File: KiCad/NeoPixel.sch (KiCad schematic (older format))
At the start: 13 parts, among them J701 NEO1, J702 5V_I/O_2, J703 5V_I/O_1, J704 NEO1, J705 NEO1, J706 NEO1, J707 NeoPixel, U701 TXB0102DCT

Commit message: Remade layout
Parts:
- removed J707: NeoPixel, Pin_Headers:Pin_Header_Straight_1x01_Pitch2.54mm, symbol CONN_01X01
- added J707: CONN_01X03, Pin_Headers:Pin_Header_Straight_1x03_Pitch2.54mm, symbol CONN_01X03
- J704: value NEO1 -> NEO2
- J705: value NEO1 -> NEO3
- J706: value NEO1 -> NEO4
- renumbered J702 to J701, J703 to J702, J701 to J703
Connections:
- net GND: now also J701.1 (P1), J702.1 (P1), J707.1 (P1); no longer J701.2 (P2), J702.2 (P2)
- net POWER5V: now also J707.2 (P2)
- net at C703.1, U701.1 (B2): now also J701.2 (P2); no longer J701.1 (P1)
- net at C704.1, J703.1, U701.8 (B1): now also J702.2 (P2); no longer J702.1 (P1)
- net at J706.4: now also J707.3 (P3)
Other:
- moved on the sheet: C703, C704, J701, J702, J703, J704, J705, J706

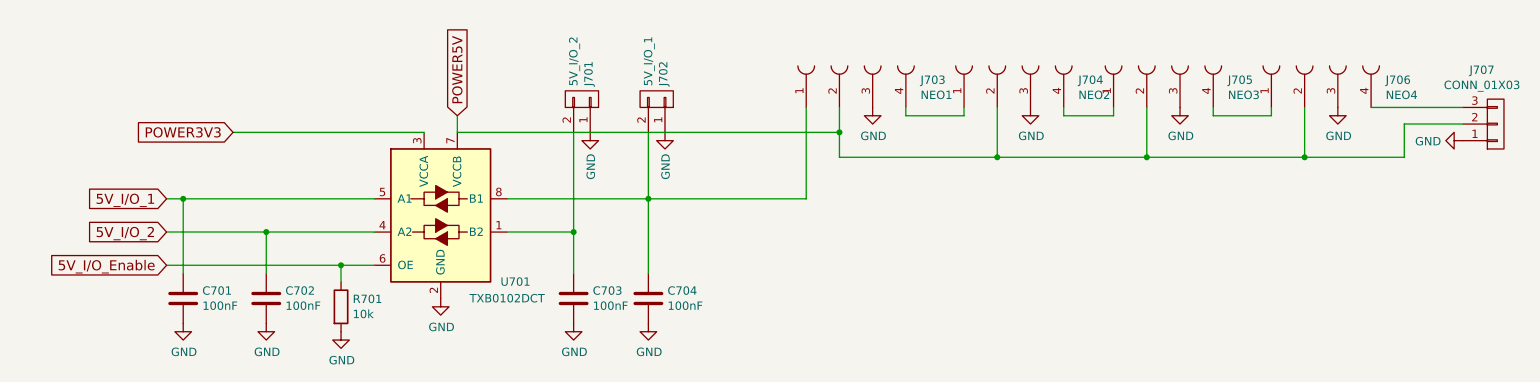
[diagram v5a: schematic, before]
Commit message: New sense input circuits. New layout
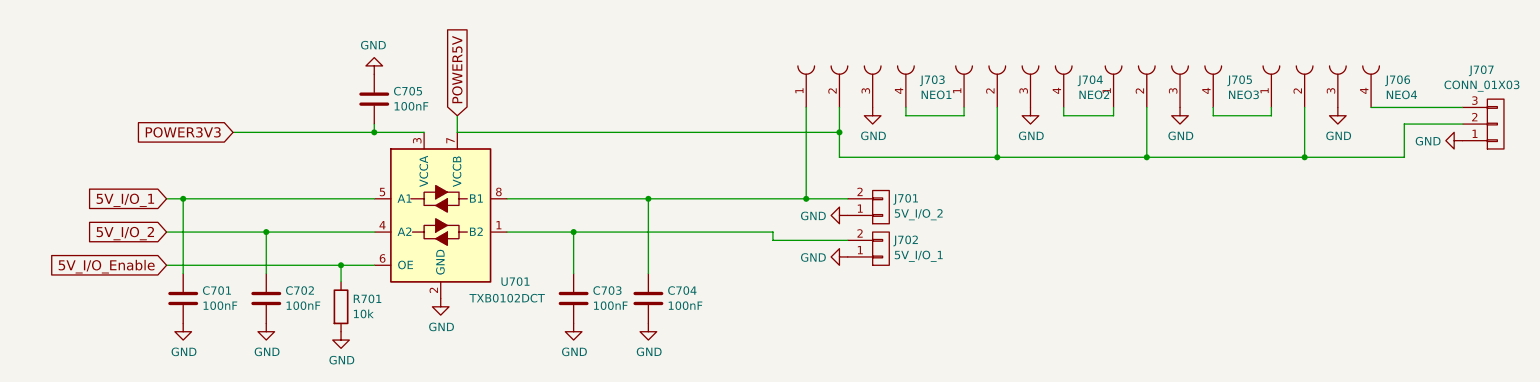
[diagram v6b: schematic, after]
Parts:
- added C705: 100nF, Capacitors_SMD:C_0805, symbol C
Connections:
- net GND: now also C705.1
- net POWER3V3: now also C705.2
- net at C703.1, U701.1 (B2): now also J702.2 (P2); no longer J701.2 (P2)
- net at C704.1, J703.1, U701.8 (B1): now also J701.2 (P2); no longer J702.2 (P2)
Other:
- moved on the sheet: J701, J702
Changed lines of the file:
@@
 F 1 "TXB0102DCT" H 3450 1200 50  0000 C CNN
 F 2 "Housings_SSOP:TSSOP-8_3x3mm_Pitch0.65mm" H 4000 1100 50  0001 C CNN
-F 3 "" H 3050 1670 50  0001 C CNN
+F 3 "https://www.digikey.se/product-detail/en/texas-instruments/TXB0102DCUR/296-22862-1-ND/1740009" H 3050 1670 50  0001 C CNN
 	1    3050 1700
 	1    0    0    -1
@@
 POWER3V3
 $Comp
-L GND #PWR0136
+L GND #PWR0144
 U 1 1 5926005F
 P 3050 2200
-F 0 "#PWR0136" H 3050 1950 50  0001 C CNN
+F 0 "#PWR0144" H 3050 1950 50  0001 C CNN
 F 1 "GND" H 3055 2027 50  0000 C CNN
 F 2 "" H 3050 2200 50  0001 C CNN
@@
 $EndComp
 $Comp
-L GND #PWR0137
+L GND #PWR0145
 U 1 1 592606C6
 P 2450 2400
-F 0 "#PWR0137" H 2450 2150 50  0001 C CNN
+F 0 "#PWR0145" H 2450 2150 50  0001 C CNN
 F 1 "GND" H 2455 2227 50  0000 C CNN
 F 2 "" H 2450 2400 50  0001 C CNN
@@
 $EndComp
 $Comp
-L GND #PWR0138
+L GND #PWR0146
 U 1 1 59260916
 P 2000 2350
-F 0 "#PWR0138" H 2000 2100 50  0001 C CNN
+F 0 "#PWR0146" H 2000 2100 50  0001 C CNN
 F 1 "GND" H 2005 2177 50  0000 C CNN
 F 2 "" H 2000 2350 50  0001 C CNN
@@
 $EndComp
 $Comp
-L GND #PWR0139
+L GND #PWR0147
 U 1 1 592609AA
 P 1500 2350
-F 0 "#PWR0139" H 1500 2100 50  0001 C CNN
+F 0 "#PWR0147" H 1500 2100 50  0001 C CNN
 F 1 "GND" H 1505 2177 50  0000 C CNN
 F 2 "" H 1500 2350 50  0001 C CNN
@@
 $EndComp
 $Comp
-L GND #PWR0140
+L GND #PWR0148
 U 1 1 59260BC2
 P 3850 2350
-F 0 "#PWR0140" H 3850 2100 50  0001 C CNN
+F 0 "#PWR0148" H 3850 2100 50  0001 C CNN
 F 1 "GND" H 3855 2177 50  0000 C CNN
 F 2 "" H 3850 2350 50  0001 C CNN
@@
 $EndComp
 $Comp
-L GND #PWR0141
+L GND #PWR0149
 U 1 1 59260BD9
 P 4300 2350
-F 0 "#PWR0141" H 4300 2100 50  0001 C CNN
+F 0 "#PWR0149" H 4300 2100 50  0001 C CNN
 F 1 "GND" H 4305 2177 50  0000 C CNN
 F 2 "" H 4300 2350 50  0001 C CNN
@@
 L CONN_01X02 J702
 U 1 1 59260CEC
-P 4350 1000
-F 0 "J702" H 4428 1041 50  0000 L CNN
-F 1 "5V_I/O_1" H 4428 950 50  0000 L CNN
-F 2 "Pin_Headers:Pin_Header_Straight_1x02_Pitch2.54mm" H 4350 1000 50  0001 C CNN
-F 3 "" H 4350 1000 50  0001 C CNN
-	1    4350 1000
-	0    1    -1   0
+P 5700 1900
+F 0 "J702" H 5778 1849 50  0000 L CNN
+F 1 "5V_I/O_1" H 5778 1940 50  0000 L CNN
+F 2 "Pin_Headers:Pin_Header_Straight_1x02_Pitch2.54mm" H 5700 1900 50  0001 C CNN
+F 3 "" H 5700 1900 50  0001 C CNN
+	1    5700 1900
+	1    0    0    1
 $EndComp
 $Comp
 L CONN_01X02 J701
 U 1 1 59260D8E
-P 3900 1000
-F 0 "J701" H 3978 1041 50  0000 L CNN
-F 1 "5V_I/O_2" H 3978 950 50  0000 L CNN
-F 2 "Pin_Headers:Pin_Header_Straight_1x02_Pitch2.54mm" H 3900 1000 50  0001 C CNN
-F 3 "" H 3900 1000 50  0001 C CNN
-	1    3900 1000
-	0    1    -1   0
-$EndComp
-$Comp
-L GND #PWR0142
+P 5700 1650
+F 0 "J701" H 5778 1599 50  0000 L CNN
+F 1 "5V_I/O_2" H 5778 1690 50  0000 L CNN
+F 2 "Pin_Headers:Pin_Header_Straight_1x02_Pitch2.54mm" H 5700 1650 50  0001 C CNN
+F 3 "" H 5700 1650 50  0001 C CNN
+	1    5700 1650
+	1    0    0    1
+$EndComp
+$Comp
+L GND #PWR0150
 U 1 1 59260EBE
-P 3950 1200
-F 0 "#PWR0142" H 3950 950 50  0001 C CNN
-F 1 "GND" V 3955 1072 50  0000 R CNN
-F 2 "" H 3950 1200 50  0001 C CNN
-F 3 "" H 3950 1200 50  0001 C CNN
-	1    3950 1200
-	1    0    0    -1
-$EndComp
-$Comp
-L GND #PWR0143
+P 5500 1700
+F 0 "#PWR0150" H 5500 1450 50  0001 C CNN
+F 1 "GND" V 5505 1572 50  0000 R CNN
+F 2 "" H 5500 1700 50  0001 C CNN
+F 3 "" H 5500 1700 50  0001 C CNN
+	1    5500 1700
+	0    1    1    0
+$EndComp
+$Comp
+L GND #PWR0151
 U 1 1 59260EE1
-P 4400 1200
-F 0 "#PWR0143" H 4400 950 50  0001 C CNN
-F 1 "GND" V 4405 1072 50  0000 R CNN
-F 2 "" H 4400 1200 50  0001 C CNN
-F 3 "" H 4400 1200 50  0001 C CNN
-	1    4400 1200
-	1    0    0    -1
+P 5500 1950
+F 0 "#PWR0151" H 5500 1700 50  0001 C CNN
+F 1 "GND" V 5505 1822 50  0000 R CNN
+F 2 "" H 5500 1950 50  0001 C CNN
+F 3 "" H 5500 1950 50  0001 C CNN
+	1    5500 1950
+	0    1    1    0
 $EndComp
 $Comp
@@
 $EndComp
 $Comp
-L GND #PWR0144
+L GND #PWR0152
 U 1 1 5926162B
 P 5650 1050
-F 0 "#PWR0144" H 5650 800 50  0001 C CNN
+F 0 "#PWR0152" H 5650 800 50  0001 C CNN
 F 1 "GND" H 5655 877 50  0000 C CNN
 F 2 "" H 5650 1050 50  0001 C CNN
@@
 $EndComp
 $Comp
-L GND #PWR0145
+L GND #PWR0153
 U 1 1 59261C0C
 P 6600 1050
-F 0 "#PWR0145" H 6600 800 50  0001 C CNN
+F 0 "#PWR0153" H 6600 800 50  0001 C CNN
 F 1 "GND" H 6605 877 50  0000 C CNN
 F 2 "" H 6600 1050 50  0001 C CNN
@@
 $EndComp
 $Comp
-L GND #PWR0146
+L GND #PWR0154
 U 1 1 59261C2F
 P 7500 1050
-F 0 "#PWR0146" H 7500 800 50  0001 C CNN
+F 0 "#PWR0154" H 7500 800 50  0001 C CNN
 F 1 "GND" H 7505 877 50  0000 C CNN
 F 2 "" H 7500 1050 50  0001 C CNN
@@
 $EndComp
 $Comp
-L GND #PWR0147
+L GND #PWR0155
 U 1 1 59261C52
 P 8450 1050
-F 0 "#PWR0147" H 8450 800 50  0001 C CNN
+F 0 "#PWR0155" H 8450 800 50  0001 C CNN
 F 1 "GND" H 8455 877 50  0000 C CNN
 F 2 "" H 8450 1050 50  0001 C CNN
@@
 Connection ~ 1500 1600
 Wire Wire Line
-	3450 1800 3850 1800
-Wire Wire Line
-	3850 1200 3850 2050
-Wire Wire Line
-	3450 1600 5250 1600
-Wire Wire Line
-	4300 1200 4300 2050
-Connection ~ 4300 1600
+	3450 1800 5050 1800
+Wire Wire Line
+	3850 1800 3850 2050
+Wire Wire Line
+	3450 1600 5500 1600
 Connection ~ 3850 1800
 Wire Wire Line
@@
 	9200 1050 8650 1050
 $Comp
-L GND #PWR0148
+L GND #PWR0156
 U 1 1 59280C13
 P 9200 1250
-F 0 "#PWR0148" H 9200 1000 50  0001 C CNN
+F 0 "#PWR0156" H 9200 1000 50  0001 C CNN
 F 1 "GND" V 9205 1122 50  0000 R CNN
 F 2 "" H 9200 1250 50  0001 C CNN
@@
 	8850 1150 9200 1150
 Connection ~ 8250 1350
+$Comp
+L C C705
+U 1 1 5938371E
+P 2650 1000
+F 0 "C705" H 2765 1046 50  0000 L CNN
+F 1 "100nF" H 2765 955 50  0000 L CNN
+F 2 "Capacitors_SMD:C_0805" H 2688 850 50  0001 C CNN
+F 3 "" H 2650 1000 50  0001 C CNN
+	1    2650 1000
+	1    0    0    -1
+$EndComp
+Wire Wire Line
+	2650 1150 2650 1200
+Connection ~ 2650 1200
+$Comp
+L GND #PWR0157
+U 1 1 593838B5
+P 2650 850
+F 0 "#PWR0157" H 2650 600 50  0001 C CNN
+F 1 "GND" H 2655 677 50  0000 C CNN
+F 2 "" H 2650 850 50  0001 C CNN
+F 3 "" H 2650 850 50  0001 C CNN
+	1    2650 850
+	-1   0    0    1
+$EndComp
+Wire Wire Line
+	4300 2050 4300 1600
+Connection ~ 4300 1600
+Connection ~ 5250 1600
+Wire Wire Line
+	5050 1800 5050 1850
+Wire Wire Line
+	5050 1850 5500 1850
 $EndSCHEMATC

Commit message: Starting another routing pass
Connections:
- net 5V_I/O_1 renamed 5V_IO_1
- net 5V_I/O_2 renamed 5V_IO_2
- net 5V_I/O_Enable renamed 5V_IO_Enable
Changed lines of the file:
@@
 POWER3V3
 $Comp
-L GND #PWR0144
+L GND #PWR0142
 U 1 1 5926005F
 P 3050 2200
-F 0 "#PWR0144" H 3050 1950 50  0001 C CNN
+F 0 "#PWR0142" H 3050 1950 50  0001 C CNN
 F 1 "GND" H 3055 2027 50  0000 C CNN
 F 2 "" H 3050 2200 50  0001 C CNN
@@
 $EndComp
 Text GLabel 1400 1800 0    60   Input ~ 0
-5V_I/O_2
+5V_IO_2
 Text GLabel 1400 1600 0    60   Input ~ 0
-5V_I/O_1
+5V_IO_1
 Text GLabel 1400 2000 0    60   Input ~ 0
-5V_I/O_Enable
+5V_IO_Enable
 $Comp
 L R R701
@@
 $EndComp
 $Comp
-L GND #PWR0145
+L GND #PWR0143
 U 1 1 592606C6
 P 2450 2400
-F 0 "#PWR0145" H 2450 2150 50  0001 C CNN
+F 0 "#PWR0143" H 2450 2150 50  0001 C CNN
 F 1 "GND" H 2455 2227 50  0000 C CNN
 F 2 "" H 2450 2400 50  0001 C CNN
@@
 $EndComp
 $Comp
-L GND #PWR0146
+L GND #PWR0144
 U 1 1 59260916
 P 2000 2350
-F 0 "#PWR0146" H 2000 2100 50  0001 C CNN
+F 0 "#PWR0144" H 2000 2100 50  0001 C CNN
 F 1 "GND" H 2005 2177 50  0000 C CNN
 F 2 "" H 2000 2350 50  0001 C CNN
@@
 $EndComp
 $Comp
-L GND #PWR0147
+L GND #PWR0145
 U 1 1 592609AA
 P 1500 2350
-F 0 "#PWR0147" H 1500 2100 50  0001 C CNN
+F 0 "#PWR0145" H 1500 2100 50  0001 C CNN
 F 1 "GND" H 1505 2177 50  0000 C CNN
 F 2 "" H 1500 2350 50  0001 C CNN
@@
 $EndComp
 $Comp
-L GND #PWR0148
+L GND #PWR0146
 U 1 1 59260BC2
 P 3850 2350
-F 0 "#PWR0148" H 3850 2100 50  0001 C CNN
+F 0 "#PWR0146" H 3850 2100 50  0001 C CNN
 F 1 "GND" H 3855 2177 50  0000 C CNN
 F 2 "" H 3850 2350 50  0001 C CNN
@@
 $EndComp
 $Comp
-L GND #PWR0149
+L GND #PWR0147
 U 1 1 59260BD9
 P 4300 2350
-F 0 "#PWR0149" H 4300 2100 50  0001 C CNN
+F 0 "#PWR0147" H 4300 2100 50  0001 C CNN
 F 1 "GND" H 4305 2177 50  0000 C CNN
 F 2 "" H 4300 2350 50  0001 C CNN
@@
 $EndComp
 $Comp
-L GND #PWR0150
+L GND #PWR0148
 U 1 1 59260EBE
 P 5500 1700
-F 0 "#PWR0150" H 5500 1450 50  0001 C CNN
+F 0 "#PWR0148" H 5500 1450 50  0001 C CNN
 F 1 "GND" V 5505 1572 50  0000 R CNN
 F 2 "" H 5500 1700 50  0001 C CNN
@@
 $EndComp
 $Comp
-L GND #PWR0151
+L GND #PWR0149
 U 1 1 59260EE1
 P 5500 1950
-F 0 "#PWR0151" H 5500 1700 50  0001 C CNN
+F 0 "#PWR0149" H 5500 1700 50  0001 C CNN
 F 1 "GND" V 5505 1822 50  0000 R CNN
 F 2 "" H 5500 1950 50  0001 C CNN
@@
 $EndComp
 $Comp
-L GND #PWR0152
+L GND #PWR0150
 U 1 1 5926162B
 P 5650 1050
-F 0 "#PWR0152" H 5650 800 50  0001 C CNN
+F 0 "#PWR0150" H 5650 800 50  0001 C CNN
 F 1 "GND" H 5655 877 50  0000 C CNN
 F 2 "" H 5650 1050 50  0001 C CNN
@@
 $EndComp
 $Comp
-L GND #PWR0153
+L GND #PWR0151
 U 1 1 59261C0C
 P 6600 1050
-F 0 "#PWR0153" H 6600 800 50  0001 C CNN
+F 0 "#PWR0151" H 6600 800 50  0001 C CNN
 F 1 "GND" H 6605 877 50  0000 C CNN
 F 2 "" H 6600 1050 50  0001 C CNN
@@
 $EndComp
 $Comp
-L GND #PWR0154
+L GND #PWR0152
 U 1 1 59261C2F
 P 7500 1050
-F 0 "#PWR0154" H 7500 800 50  0001 C CNN
+F 0 "#PWR0152" H 7500 800 50  0001 C CNN
 F 1 "GND" H 7505 877 50  0000 C CNN
 F 2 "" H 7500 1050 50  0001 C CNN
@@
 $EndComp
 $Comp
-L GND #PWR0155
+L GND #PWR0153
 U 1 1 59261C52
 P 8450 1050
-F 0 "#PWR0155" H 8450 800 50  0001 C CNN
+F 0 "#PWR0153" H 8450 800 50  0001 C CNN
 F 1 "GND" H 8455 877 50  0000 C CNN
 F 2 "" H 8450 1050 50  0001 C CNN
@@
 	9200 1050 8650 1050
 $Comp
-L GND #PWR0156
+L GND #PWR0154
 U 1 1 59280C13
 P 9200 1250
-F 0 "#PWR0156" H 9200 1000 50  0001 C CNN
+F 0 "#PWR0154" H 9200 1000 50  0001 C CNN
 F 1 "GND" V 9205 1122 50  0000 R CNN
 F 2 "" H 9200 1250 50  0001 C CNN
@@
 Connection ~ 2650 1200
 $Comp
-L GND #PWR0157
+L GND #PWR0155
 U 1 1 593838B5
 P 2650 850
-F 0 "#PWR0157" H 2650 600 50  0001 C CNN
+F 0 "#PWR0155" H 2650 600 50  0001 C CNN
 F 1 "GND" H 2655 677 50  0000 C CNN
 F 2 "" H 2650 850 50  0001 C CNN

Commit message: Groudplanes
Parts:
- J701: value 5V_I/O_2 -> 5V_I/O_1
- J702: value 5V_I/O_1 -> 5V_I/O_2
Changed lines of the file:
@@
 P 5700 1900
 F 0 "J702" H 5778 1849 50  0000 L CNN
-F 1 "5V_I/O_1" H 5778 1940 50  0000 L CNN
+F 1 "5V_I/O_2" H 5778 1940 50  0000 L CNN
 F 2 "Pin_Headers:Pin_Header_Straight_1x02_Pitch2.54mm" H 5700 1900 50  0001 C CNN
 F 3 "" H 5700 1900 50  0001 C CNN
@@
 P 5700 1650
 F 0 "J701" H 5778 1599 50  0000 L CNN
-F 1 "5V_I/O_2" H 5778 1690 50  0000 L CNN
+F 1 "5V_I/O_1" H 5778 1690 50  0000 L CNN
 F 2 "Pin_Headers:Pin_Header_Straight_1x02_Pitch2.54mm" H 5700 1650 50  0001 C CNN
 F 3 "" H 5700 1650 50  0001 C CNN
